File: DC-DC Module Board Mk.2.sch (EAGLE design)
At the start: 148 parts, among them U1 PCA9685, U3 LM1085IS-5.0

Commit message: pwm chip headers wired
need to give the bottom half more room so wires can come in
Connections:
- net DGND: now also UFIT4.P1, UFIT5.P1, UFIT6.P1
- net N$14: now also JP2.3; no longer JP2.2
- net N$20: now also JP2.4; no longer JP2.1
- net N$21: now also JP2.2; no longer JP2.3
- net N$24: now also JP2.1; no longer JP2.4
- net N$26: now also JP1.4; no longer JP1.1
- net N$27: now also JP1.3; no longer JP1.2
- net N$28: now also JP1.2; no longer JP1.3
- net N$29: now also JP1.1; no longer JP1.4
- net N$30: now also JP3.1; no longer JP3.4
- net N$31: now also JP3.2; no longer JP3.3
- net N$32: now also JP3.3; no longer JP3.2
- net N$37: now also JP3.4; no longer JP3.1
- net N$38: now also JP4.1; no longer JP4.4
- net N$39: now also JP4.2; no longer JP4.3
- net N$40: now also JP4.3; no longer JP4.2
- net N$41: now also JP4.4; no longer JP4.1
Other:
- note added: "had a weird disconnect problem, grid was unchanged"
- moved on the sheet: JP1, JP2, JP3, JP4
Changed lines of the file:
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@@
 <text x="330.2" y="53.34" size="1.778" layer="95">thrust8</text>
 <text x="441.96" y="172.72" size="1.778" layer="95">pwm chan 0</text>
+<text x="353.06" y="93.98" size="1.778" layer="97">had a weird
+disconnect
+problem,
+grid was
+unchanged</text>
 </plain>
 <instances>
@@
 <instance part="C22V1" gate="G$1" x="60.96" y="143.256"/>
 <instance part="C22V2" gate="G$1" x="63.5" y="70.866"/>
-<instance part="JP1" gate="A" x="-73.66" y="-91.44"/>
-<instance part="JP2" gate="A" x="-73.66" y="-73.66"/>
-<instance part="JP3" gate="A" x="-30.48" y="-91.44"/>
-<instance part="JP4" gate="A" x="-30.48" y="-73.66"/>
+<instance part="JP1" gate="A" x="-78.74" y="-88.9" rot="R180"/>
+<instance part="JP2" gate="A" x="-78.74" y="-71.12" rot="R180"/>
+<instance part="JP3" gate="A" x="-35.56" y="-88.9" rot="R180"/>
+<instance part="JP4" gate="A" x="-35.56" y="-71.12" rot="R180"/>
 </instances>
 <busses>
@@
 </segment>
 <segment>
+<wire x1="335.28" y1="124.46" x2="340.36" y2="124.46" width="0.1524" layer="91"/>
+<label x="340.36" y="124.46" size="1.27" layer="95" xref="yes"/>
+</segment>
+<segment>
+<wire x1="330.2" y1="104.14" x2="335.28" y2="104.14" width="0.1524" layer="91"/>
+<label x="335.28" y="104.14" size="1.27" layer="95" xref="yes"/>
+</segment>
+<segment>
+<wire x1="330.2" y1="83.82" x2="335.28" y2="83.82" width="0.1524" layer="91"/>
+<label x="335.28" y="83.82" size="1.27" layer="95" xref="yes"/>
+</segment>
+<segment>
+<pinref part="UFIT4" gate="G$1" pin="P1"/>
 <wire x1="322.58" y1="124.46" x2="327.66" y2="124.46" width="0.1524" layer="91"/>
-<label x="327.66" y="124.46" size="1.27" layer="95" xref="yes"/>
-</segment>
-<segment>
+<label x="325.12" y="124.46" size="1.778" layer="95"/>
+</segment>
+<segment>
+<pinref part="UFIT5" gate="G$1" pin="P1"/>
 <wire x1="322.58" y1="104.14" x2="327.66" y2="104.14" width="0.1524" layer="91"/>
-<label x="327.66" y="104.14" size="1.27" layer="95" xref="yes"/>
-</segment>
-<segment>
+<label x="322.58" y="104.14" size="1.778" layer="95"/>
+</segment>
+<segment>
+<pinref part="UFIT6" gate="G$1" pin="P1"/>
 <wire x1="322.58" y1="83.82" x2="327.66" y2="83.82" width="0.1524" layer="91"/>
-<label x="327.66" y="83.82" size="1.27" layer="95" xref="yes"/>
+<label x="322.58" y="83.82" size="1.778" layer="95"/>
 </segment>
 </net>
@@
 <wire x1="-83.82" y1="-71.12" x2="-76.2" y2="-71.12" width="0.1524" layer="91"/>
 <pinref part="RPWM6" gate="G$1" pin="1"/>
-<pinref part="JP2" gate="A" pin="2"/>
+<pinref part="JP2" gate="A" pin="3"/>
 </segment>
 </net>
@@
 <wire x1="-83.82" y1="-68.58" x2="-76.2" y2="-68.58" width="0.1524" layer="91"/>
 <pinref part="RPWM7" gate="G$1" pin="1"/>
-<pinref part="JP2" gate="A" pin="1"/>
+<pinref part="JP2" gate="A" pin="4"/>
 </segment>
 </net>
@@
 <wire x1="-83.82" y1="-73.66" x2="-76.2" y2="-73.66" width="0.1524" layer="91"/>
 <pinref part="RPWM5" gate="G$1" pin="1"/>
-<pinref part="JP2" gate="A" pin="3"/>
+<pinref part="JP2" gate="A" pin="2"/>
 </segment>
 </net>
@@
 <wire x1="-83.82" y1="-76.2" x2="-76.2" y2="-76.2" width="0.1524" layer="91"/>
 <pinref part="RPWM4" gate="G$1" pin="1"/>
-<pinref part="JP2" gate="A" pin="4"/>
+<pinref part="JP2" gate="A" pin="1"/>
 </segment>
 </net>
@@
 <wire x1="-83.82" y1="-86.36" x2="-76.2" y2="-86.36" width="0.1524" layer="91"/>
 <pinref part="RPWM3" gate="G$1" pin="1"/>
-<pinref part="JP1" gate="A" pin="1"/>
+<pinref part="JP1" gate="A" pin="4"/>
 </segment>
 </net>
@@
 <wire x1="-83.82" y1="-88.9" x2="-76.2" y2="-88.9" width="0.1524" layer="91"/>
 <pinref part="RPWM2" gate="G$1" pin="1"/>
-<pinref part="JP1" gate="A" pin="2"/>
+<pinref part="JP1" gate="A" pin="3"/>
 </segment>
 </net>
@@
 <wire x1="-83.82" y1="-91.44" x2="-76.2" y2="-91.44" width="0.1524" layer="91"/>
 <pinref part="RPWM1" gate="G$1" pin="1"/>
-<pinref part="JP1" gate="A" pin="3"/>
+<pinref part="JP1" gate="A" pin="2"/>
 </segment>
 </net>
@@
 <wire x1="-83.82" y1="-93.98" x2="-76.2" y2="-93.98" width="0.1524" layer="91"/>
 <pinref part="RPWM0" gate="G$1" pin="1"/>
-<pinref part="JP1" gate="A" pin="4"/>
+<pinref part="JP1" gate="A" pin="1"/>
 </segment>
 </net>
@@
 <wire x1="-40.64" y1="-93.98" x2="-33.02" y2="-93.98" width="0.1524" layer="91"/>
 <pinref part="RPWM8" gate="G$1" pin="1"/>
-<pinref part="JP3" gate="A" pin="4"/>
+<pinref part="JP3" gate="A" pin="1"/>
 </segment>
 </net>
@@
 <wire x1="-40.64" y1="-91.44" x2="-33.02" y2="-91.44" width="0.1524" layer="91"/>
 <pinref part="RPWM9" gate="G$1" pin="1"/>
-<pinref part="JP3" gate="A" pin="3"/>
+<pinref part="JP3" gate="A" pin="2"/>
 </segment>
 </net>
@@
 <wire x1="-40.64" y1="-88.9" x2="-33.02" y2="-88.9" width="0.1524" layer="91"/>
 <pinref part="RPWM10" gate="G$1" pin="1"/>
-<pinref part="JP3" gate="A" pin="2"/>
+<pinref part="JP3" gate="A" pin="3"/>
 </segment>
 </net>
@@
 <wire x1="-40.64" y1="-86.36" x2="-33.02" y2="-86.36" width="0.1524" layer="91"/>
 <pinref part="RPWM11" gate="G$1" pin="1"/>
-<pinref part="JP3" gate="A" pin="1"/>
+<pinref part="JP3" gate="A" pin="4"/>
 </segment>
 </net>
@@
 <wire x1="-40.64" y1="-76.2" x2="-33.02" y2="-76.2" width="0.1524" layer="91"/>
 <pinref part="RPWM12" gate="G$1" pin="1"/>
-<pinref part="JP4" gate="A" pin="4"/>
+<pinref part="JP4" gate="A" pin="1"/>
 </segment>
 </net>
@@
 <wire x1="-40.64" y1="-73.66" x2="-33.02" y2="-73.66" width="0.1524" layer="91"/>
 <pinref part="RPWM13" gate="G$1" pin="1"/>
-<pinref part="JP4" gate="A" pin="3"/>
+<pinref part="JP4" gate="A" pin="2"/>
 </segment>
 </net>
@@
 <wire x1="-40.64" y1="-71.12" x2="-33.02" y2="-71.12" width="0.1524" layer="91"/>
 <pinref part="RPWM14" gate="G$1" pin="1"/>
-<pinref part="JP4" gate="A" pin="2"/>
+<pinref part="JP4" gate="A" pin="3"/>
 </segment>
 </net>
@@
 <wire x1="-40.64" y1="-68.58" x2="-33.02" y2="-68.58" width="0.1524" layer="91"/>
 <pinref part="RPWM15" gate="G$1" pin="1"/>
-<pinref part="JP4" gate="A" pin="1"/>
+<pinref part="JP4" gate="A" pin="4"/>
 </segment>
 </net>
@@
 </schematic>
 </drawing>
+<compatibility>
+<note version="6.3" minversion="6.2.2" severity="warning">
+Since Version 6.2.2 text objects can contain more than one line,
+which will not be processed correctly with this version.
+</note>
+</compatibility>
 </eagle>

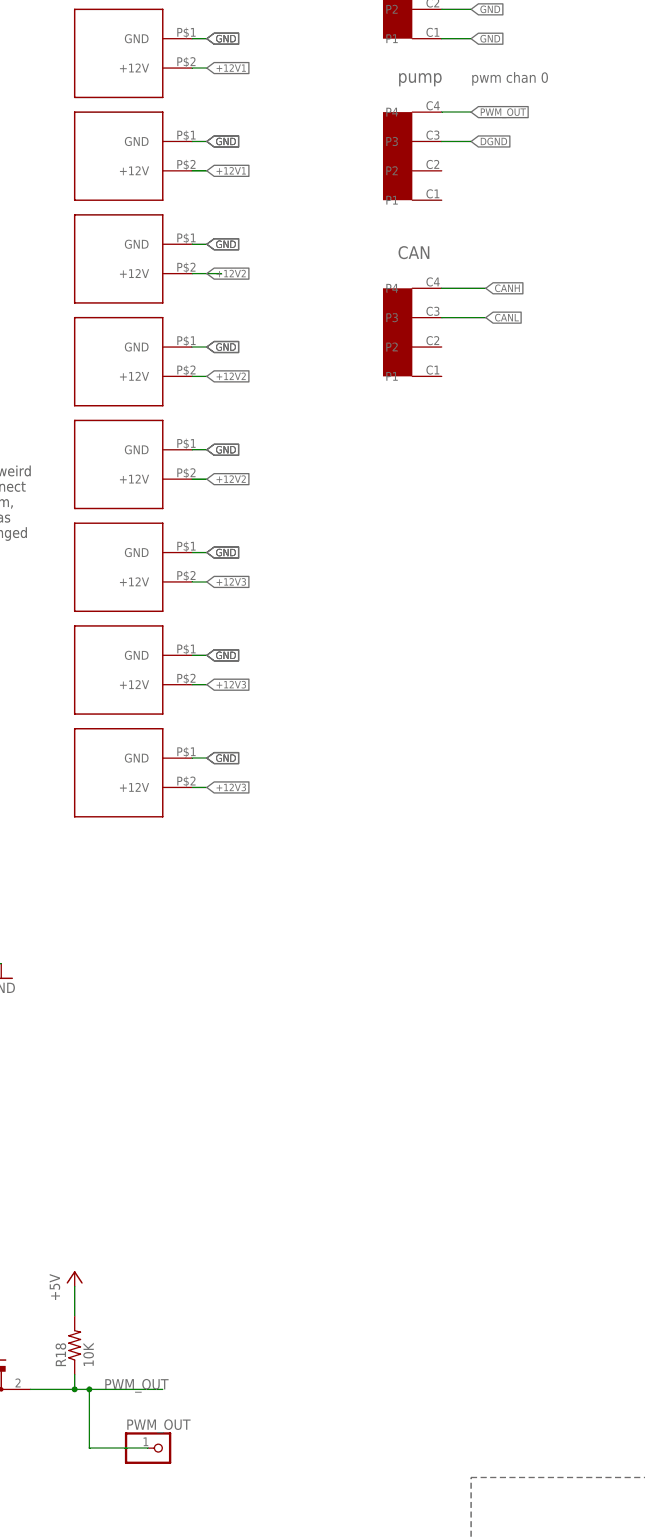
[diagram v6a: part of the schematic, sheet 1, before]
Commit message: fixed a few DRC issues, added vias for pwm chans
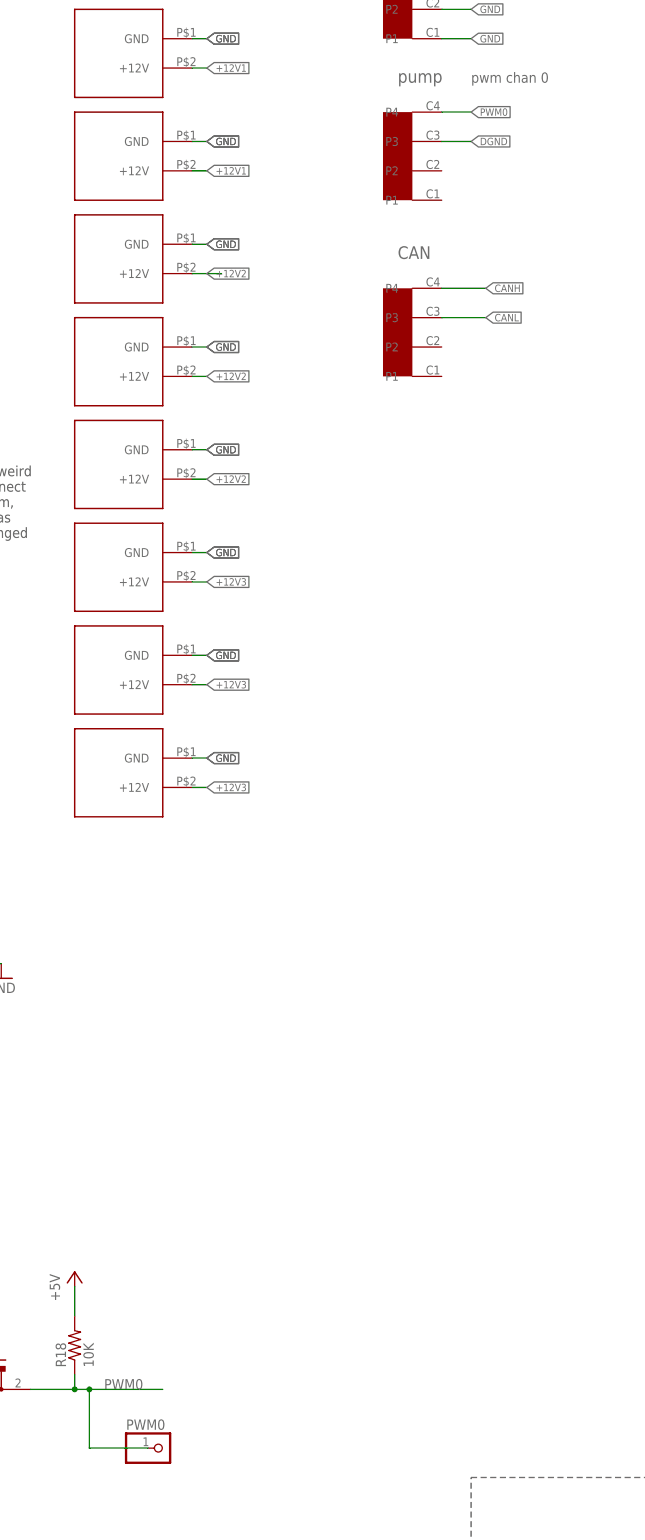
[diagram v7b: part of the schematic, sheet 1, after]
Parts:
- renumbered PWM_OUT to PWM0
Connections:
- removed net PWM_OUT: PWM0.1, R18.1, U$12.D, UFIT2.P4
- net PWM0: now also PWM0.1, R18.1, U$12.D, UFIT2.P4
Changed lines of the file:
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@@
 <part name="P+1" library="supply1" deviceset="+5V" device=""/>
 <part name="PWM_OUT_3V3" library="pinhead" deviceset="PINHD-1X1" device=""/>
-<part name="PWM_OUT" library="pinhead" deviceset="PINHD-1X1" device=""/>
+<part name="PWM0" library="pinhead" deviceset="PINHD-1X1" device=""/>
 <part name="CAN_TX" library="pinhead" deviceset="PINHD-1X1" device=""/>
 <part name="CAN_RX" library="pinhead" deviceset="PINHD-1X1" device=""/>
@@
 <instance part="P+1" gate="1" x="373.38" y="-33.02"/>
 <instance part="PWM_OUT_3V3" gate="G$1" x="347.98" y="-63.5"/>
-<instance part="PWM_OUT" gate="G$1" x="388.62" y="-63.5"/>
+<instance part="PWM0" gate="G$1" x="388.62" y="-63.5"/>
 <instance part="CAN_TX" gate="G$1" x="464.82" y="-88.9" rot="R180"/>
 <instance part="CAN_RX" gate="G$1" x="464.82" y="-106.68" rot="R180"/>
@@
 </segment>
 </net>
-<net name="PWM_OUT" class="0">
-<segment>
-<pinref part="R18" gate="G$1" pin="1"/>
-<wire x1="373.38" y1="-53.34" x2="375.92" y2="-53.34" width="0.1524" layer="91"/>
-<wire x1="375.92" y1="-53.34" x2="388.62" y2="-53.34" width="0.1524" layer="91"/>
-<wire x1="373.38" y1="-50.8" x2="373.38" y2="-53.34" width="0.1524" layer="91"/>
-<pinref part="U$12" gate="G$1" pin="D"/>
-<wire x1="365.76" y1="-53.34" x2="373.38" y2="-53.34" width="0.1524" layer="91"/>
-<junction x="373.38" y="-53.34"/>
-<label x="378.46" y="-53.34" size="1.778" layer="95"/>
-<wire x1="375.92" y1="-53.34" x2="375.92" y2="-63.5" width="0.1524" layer="91"/>
-<junction x="375.92" y="-53.34"/>
-<pinref part="PWM_OUT" gate="G$1" pin="1"/>
-<wire x1="375.92" y1="-63.5" x2="386.08" y2="-63.5" width="0.1524" layer="91"/>
-</segment>
-<segment>
-<pinref part="UFIT2" gate="G$1" pin="P4"/>
-<wire x1="436.88" y1="167.64" x2="441.96" y2="167.64" width="0.1524" layer="91"/>
-<label x="441.96" y="167.64" size="1.27" layer="95" xref="yes"/>
-</segment>
-</net>
 <net name="PWM_IN" class="0">
 <segment>
@@
 <pinref part="RPWM0" gate="G$1" pin="2"/>
 </segment>
-</net>
+<segment>
+<pinref part="R18" gate="G$1" pin="1"/>
+<wire x1="373.38" y1="-53.34" x2="375.92" y2="-53.34" width="0.1524" layer="91"/>
+<wire x1="375.92" y1="-53.34" x2="388.62" y2="-53.34" width="0.1524" layer="91"/>
+<wire x1="373.38" y1="-50.8" x2="373.38" y2="-53.34" width="0.1524" layer="91"/>
+<pinref part="U$12" gate="G$1" pin="D"/>
+<wire x1="365.76" y1="-53.34" x2="373.38" y2="-53.34" width="0.1524" layer="91"/>
+<junction x="373.38" y="-53.34"/>
+<label x="378.46" y="-53.34" size="1.778" layer="95"/>
+<wire x1="375.92" y1="-53.34" x2="375.92" y2="-63.5" width="0.1524" layer="91"/>
+<junction x="375.92" y="-53.34"/>
+<pinref part="PWM0" gate="G$1" pin="1"/>
+<wire x1="375.92" y1="-63.5" x2="386.08" y2="-63.5" width="0.1524" layer="91"/>
+</segment>
+<segment>
+<pinref part="UFIT2" gate="G$1" pin="P4"/>
+<wire x1="436.88" y1="167.64" x2="441.96" y2="167.64" width="0.1524" layer="91"/>
+<label x="441.96" y="167.64" size="1.27" layer="95" xref="yes"/>
+</segment>
+</net>

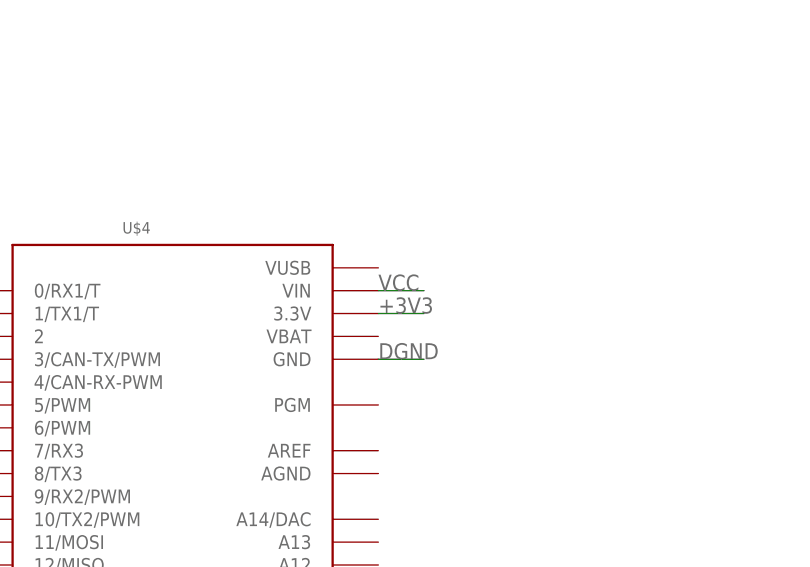
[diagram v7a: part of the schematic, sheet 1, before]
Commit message: finished tracing, fixed bugs, added info, moved sparrow
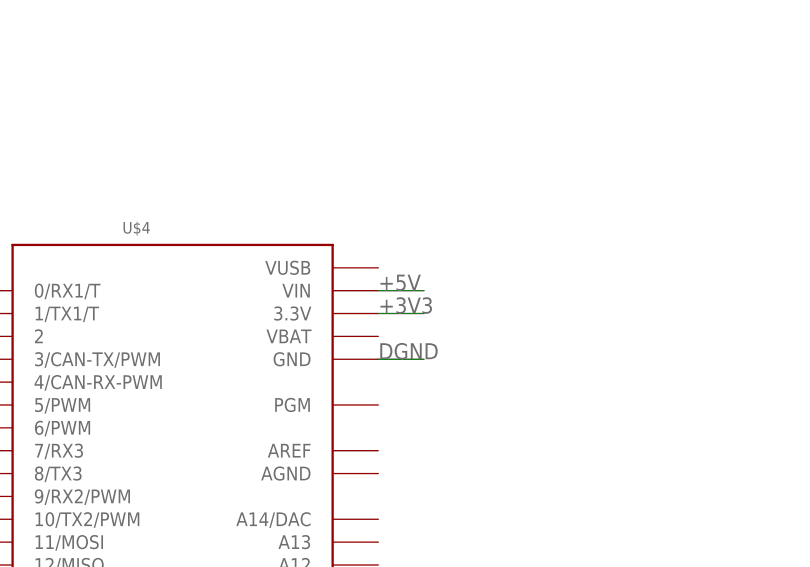
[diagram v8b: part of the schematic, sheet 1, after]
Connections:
- removed net 5.0V: JP7.1
- removed net VCC: C3.P$1, JP7.2, LED8.A, R34.2, R35.2, U$4.VIN, U1.VDD
- net +5V: now also C3.P$1, JP7.1, JP7.2, LED8.A, R34.2, R35.2, U$4.VIN, U1.VDD
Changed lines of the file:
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@@
 <wire x1="373.38" y1="-35.56" x2="373.38" y2="-40.64" width="0.1524" layer="91"/>
+</segment>
+<segment>
+<wire x1="-210.82" y1="-177.8" x2="-200.66" y2="-177.8" width="0.1524" layer="91"/>
+<pinref part="JP7" gate="A" pin="1"/>
+<pinref part="U$105" gate="G$1" pin="5.0V"/>
+</segment>
+<segment>
+<wire x1="-180.34" y1="-88.9" x2="-180.34" y2="-91.44" width="0.1524" layer="91"/>
+<wire x1="-180.34" y1="-91.44" x2="-180.34" y2="-93.98" width="0.1524" layer="91"/>
+<wire x1="-180.34" y1="-91.44" x2="-160.02" y2="-91.44" width="0.1524" layer="91"/>
+<junction x="-180.34" y="-91.44"/>
+<pinref part="P+6" gate="VCC" pin="VCC"/>
+<pinref part="C3" gate="G$1" pin="P$1"/>
+<pinref part="U1" gate="G$1" pin="VDD"/>
+</segment>
+<segment>
+<wire x1="-200.66" y1="-180.34" x2="-213.36" y2="-180.34" width="0.1524" layer="91"/>
+<wire x1="-213.36" y1="-180.34" x2="-213.36" y2="-157.48" width="0.1524" layer="91"/>
+<wire x1="-213.36" y1="-157.48" x2="-213.36" y2="-152.4" width="0.1524" layer="91"/>
+<wire x1="-213.36" y1="-157.48" x2="-208.28" y2="-157.48" width="0.1524" layer="91"/>
+<junction x="-213.36" y="-157.48"/>
+<pinref part="P+11" gate="VCC" pin="VCC"/>
+<pinref part="LED8" gate="G$1" pin="A"/>
+<pinref part="JP7" gate="A" pin="2"/>
+</segment>
+<segment>
+<wire x1="-228.6" y1="-170.18" x2="-228.6" y2="-167.64" width="0.1524" layer="91"/>
+<pinref part="R35" gate="G$1" pin="2"/>
+<pinref part="P+13" gate="VCC" pin="VCC"/>
+</segment>
+<segment>
+<wire x1="-220.98" y1="-170.18" x2="-220.98" y2="-167.64" width="0.1524" layer="91"/>
+<pinref part="R34" gate="G$1" pin="2"/>
+<pinref part="P+12" gate="VCC" pin="VCC"/>
+</segment>
+<segment>
+<pinref part="U$4" gate="G$1" pin="VIN"/>
+<wire x1="246.38" y1="-27.94" x2="251.46" y2="-27.94" width="0.1524" layer="91"/>
+<label x="246.38" y="-27.94" size="1.778" layer="95"/>
 </segment>
 </net>
@@
 </segment>
 </net>
-<net name="5.0V" class="0">
-<segment>
-<wire x1="-210.82" y1="-177.8" x2="-200.66" y2="-177.8" width="0.1524" layer="91"/>
-<pinref part="JP7" gate="A" pin="1"/>
-<pinref part="U$105" gate="G$1" pin="5.0V"/>
-</segment>
-</net>
 <net name="A0" class="0">
 <segment>
@@
 </segment>
 </net>
-<net name="VCC" class="0">
-<segment>
-<wire x1="-180.34" y1="-88.9" x2="-180.34" y2="-91.44" width="0.1524" layer="91"/>
-<wire x1="-180.34" y1="-91.44" x2="-180.34" y2="-93.98" width="0.1524" layer="91"/>
-<wire x1="-180.34" y1="-91.44" x2="-160.02" y2="-91.44" width="0.1524" layer="91"/>
-<junction x="-180.34" y="-91.44"/>
-<pinref part="P+6" gate="VCC" pin="VCC"/>
-<pinref part="C3" gate="G$1" pin="P$1"/>
-<pinref part="U1" gate="G$1" pin="VDD"/>
-</segment>
-<segment>
-<wire x1="-200.66" y1="-180.34" x2="-213.36" y2="-180.34" width="0.1524" layer="91"/>
-<wire x1="-213.36" y1="-180.34" x2="-213.36" y2="-157.48" width="0.1524" layer="91"/>
-<wire x1="-213.36" y1="-157.48" x2="-213.36" y2="-152.4" width="0.1524" layer="91"/>
-<wire x1="-213.36" y1="-157.48" x2="-208.28" y2="-157.48" width="0.1524" layer="91"/>
-<junction x="-213.36" y="-157.48"/>
-<pinref part="P+11" gate="VCC" pin="VCC"/>
-<pinref part="LED8" gate="G$1" pin="A"/>
-<pinref part="JP7" gate="A" pin="2"/>
-</segment>
-<segment>
-<wire x1="-228.6" y1="-170.18" x2="-228.6" y2="-167.64" width="0.1524" layer="91"/>
-<pinref part="R35" gate="G$1" pin="2"/>
-<pinref part="P+13" gate="VCC" pin="VCC"/>
-</segment>
-<segment>
-<wire x1="-220.98" y1="-170.18" x2="-220.98" y2="-167.64" width="0.1524" layer="91"/>
-<pinref part="R34" gate="G$1" pin="2"/>
-<pinref part="P+12" gate="VCC" pin="VCC"/>
-</segment>
-<segment>
-<pinref part="U$4" gate="G$1" pin="VIN"/>
-<wire x1="246.38" y1="-27.94" x2="251.46" y2="-27.94" width="0.1524" layer="91"/>
-<label x="246.38" y="-27.94" size="1.778" layer="95"/>
-</segment>
-</net>
